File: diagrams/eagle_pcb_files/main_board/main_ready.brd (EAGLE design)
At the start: 67 x 31.5 mm, 31 parts

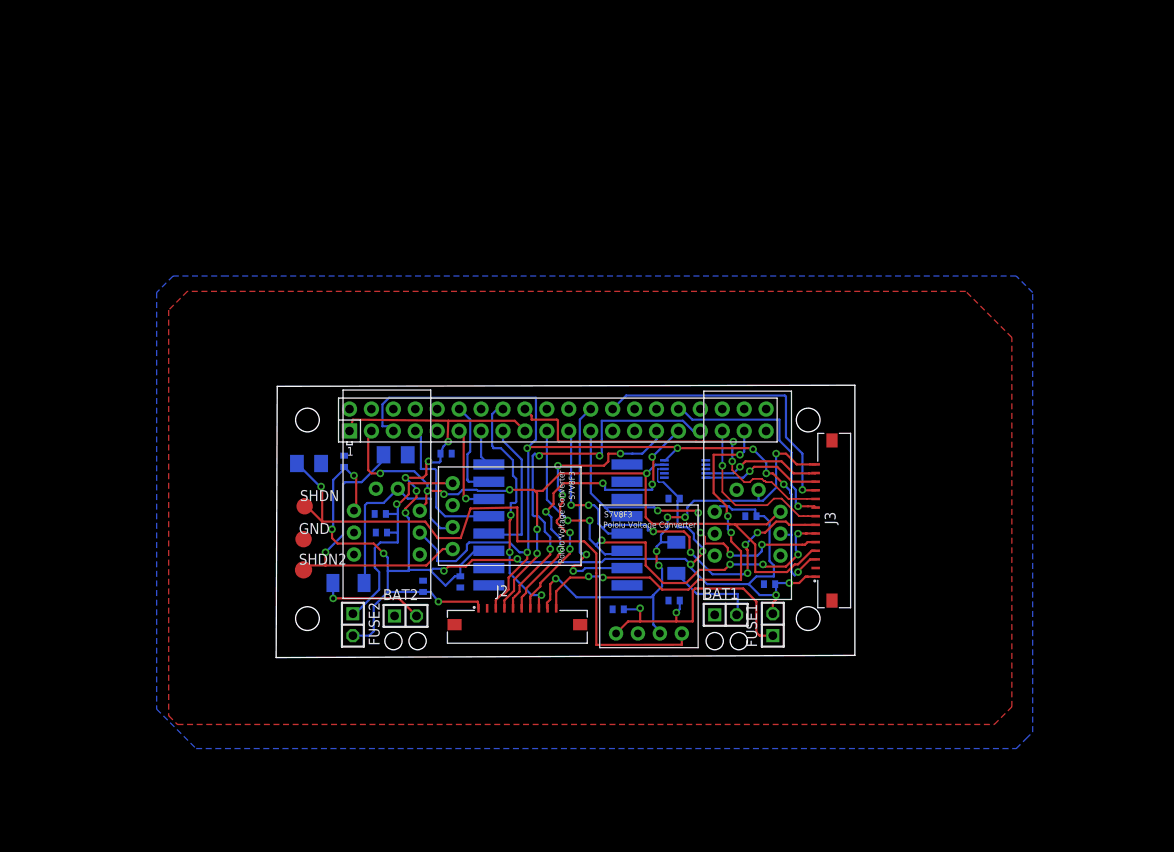
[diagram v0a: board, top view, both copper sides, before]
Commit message: Main board with wider routes and slightly less vias
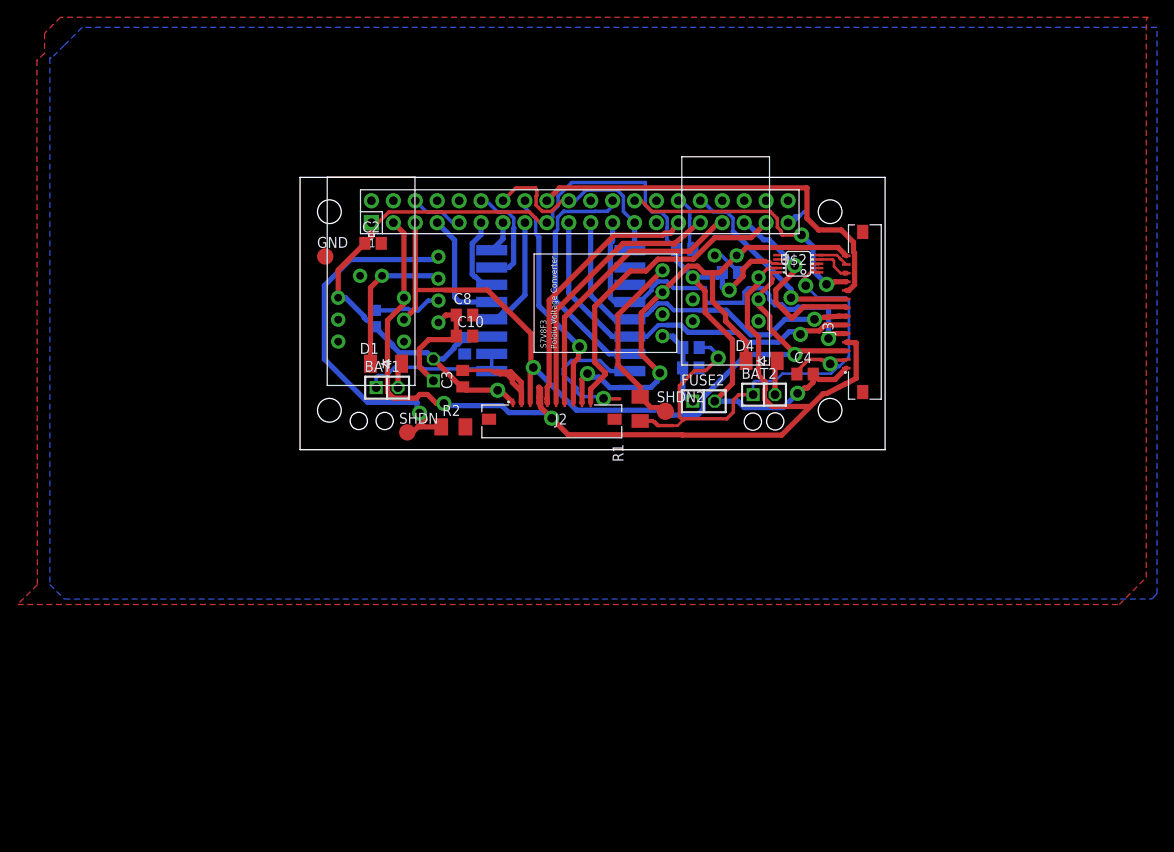
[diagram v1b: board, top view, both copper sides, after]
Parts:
- C1, C2, C3, C4, C6, C7: value (none) -> 100nF; device rcl:C0402 -> rcl:C0805
- C10, C11, C8, C9: device rcl:C0402 -> rcl:C0805
- C5: value 100 nF -> 100nF; device rcl:C0402 -> rcl:C0805
- R1, R2: value (none) -> 4.7k
- moved D4 54.3 mm to (108.2, 37.2), flipped to the top
- moved U$3 50.2 mm to (62.9, 38.1)
- moved C7 49.2 mm to (63.3, 42.1), turned to 90 degrees
- moved FUSE1 49.2 mm to (70.2, 36.1), flipped to the bottom
- moved BAT2 48.8 mm to (108.5, 33.2)
- moved FUSE2 48.2 mm to (101.5, 32.5), turned to 0 degrees
- moved U$9 47.6 mm to (104.0, 40.5)
- moved BAT1 47.2 mm to (64.8, 34.1)
- moved C6 46.5 mm to (99.3, 50.1), turned to 180 degrees
- moved SHDN2 45.8 mm to (97.0, 31.3)
- moved C8 41.0 mm to (73.8, 42.5), flipped to the top
- moved C9 40.8 mm to (100.0, 38.7), turned to 0 degrees
- moved C11 40.6 mm to (100.0, 36.3), turned to 0 degrees
- moved D1 40.5 mm to (64.7, 36.8), flipped to the top, turned to 0 degrees
- moved RAO3 38.0 mm to (77.1, 45.4), flipped to the bottom, turned to 90 degrees
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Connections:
- net A0: now also J3.12; no longer J3.13
- net A1: now also J3.13; no longer J3.12
- net B1: now also RAO2.33; no longer RAO2.29
- net B3: now also RAO2.29; no longer RAO2.33
- net GND: now also RAO2.14, U$2.1
- net VIN1: no longer J2.9, J3.14
- net VIN2: now also J2.9, J3.14
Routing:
- net GND: track 0.00 -> 176.1 mm, vias 0 -> 4
- net 3.3V: track 190.3 -> 144.9 mm, vias 15 -> 3
- net VIN1: track 57.9 -> 17.4 mm, vias 6 -> 0
- net VIN2: track 23.3 -> 61.4 mm, vias 0 -> 2
- net SHDN: track 72.3 -> 43.7 mm
- net SCL: track 115.1 -> 90.7 mm, vias 7 -> 2
- net SDA: track 96.6 -> 116.0 mm, vias 7 -> 2
- net VOUT1: track 32.8 -> 14.1 mm, vias 2 -> 0
- net VOUT2: track 27.5 -> 9.97 mm, vias 1 -> 0
- net SHDN2: track 35.0 -> 21.5 mm, vias 1 -> 0
- net B3: track 44.8 -> 31.4 mm, vias 3 -> 0
- net BUZ: track 47.1 -> 36.2 mm, vias 5 -> 0
- net A1: track 14.0 -> 3.67 mm, vias 1 -> 0
- net MOSI: track 54.9 -> 44.9 mm, vias 7 -> 1
- net A0: track 13.9 -> 4.22 mm, vias 1 -> 0
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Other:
- board size 67 x 31.5 mm -> 67.8 x 31.5 mm

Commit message: prepare main board for production
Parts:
- moved C5 1.42 mm to (103.1, 47.4)
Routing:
- net GND: track 176.1 -> 190.1 mm, vias 4 -> 5
- net DIO1: track 9.23 -> 11.0 mm
- net 3.3V: track 144.9 -> 146.6 mm
- net SCK: track 46.3 -> 47.5 mm
- net RESET: track 13.4 -> 14.2 mm
- net G3: track 47.0 -> 47.7 mm
- net G1: track 22.6 -> 22.0 mm

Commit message: make board-schematic consistent
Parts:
- FUSE1, FUSE2: value (none) -> 1.5A
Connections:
- removed net 5V0@1: RAO2.2
- removed net 5V0@2: RAO2.4
- removed net RX: RAO2.10
- removed net TX: RAO2.8
- new net 5V: RAO2.2, RAO2.4
- net GND: no longer U$2.1
- net VIN2: no longer J2.9, J3.14
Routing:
- net VIN2: track 61.4 -> 37.4 mm, vias 2 -> 1
- net GND: track 190.1 -> 185.7 mm
- net A0: track 4.22 -> 0.00 mm
- net A1: track 3.81 -> 0.00 mm
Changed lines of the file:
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@@
 <attribute name="VALUE" x="105.1306" y="34.7472" size="1.27" layer="27"/>
 </element>
-<element name="FUSE1" library="pinhead" package="1X02" value="" x="70.1548" y="36.1188" smashed="yes" rot="MR90">
+<element name="FUSE1" library="pinhead" package="1X02" value="1.5A" x="70.1548" y="36.1188" smashed="yes" rot="MR90">
 <attribute name="NAME" x="71.9836" y="33.5026" size="1.27" layer="26" ratio="10" rot="MR90"/>
 <attribute name="VALUE" x="66.9798" y="33.5788" size="1.27" layer="28" rot="MR90"/>
 </element>
-<element name="FUSE2" library="pinhead" package="1X02" value="" x="101.473" y="32.4866" smashed="yes">
+<element name="FUSE2" library="pinhead" package="1X02" value="1.5A" x="101.473" y="32.4866" smashed="yes">
 <attribute name="NAME" x="98.8568" y="34.3154" size="1.27" layer="25" ratio="10"/>
 <attribute name="VALUE" x="98.933" y="29.3116" size="1.27" layer="27"/>
@@
 <contactref element="C4" pad="1"/>
 <contactref element="J3" pad="2"/>
-<contactref element="U$2" pad="3"/>
 <contactref element="C5" pad="1"/>
 <contactref element="GND" pad="TP"/>
@@
 <contactref element="RAO1" pad="9"/>
 <contactref element="RAO1" pad="16"/>
-<contactref element="U$2" pad="1"/>
 <contactref element="RAO2" pad="9"/>
 <contactref element="RAO2" pad="39"/>
@@
 <wire x1="81.9912" y1="57.2008" x2="81.8642" y2="57.2008" width="0.4064" layer="1"/>
 <wire x1="81.8642" y1="57.2008" x2="79.7108" y2="57.2008" width="0.4064" layer="1"/>
-<wire x1="79.7108" y1="57.2008" x2="78.22" y2="55.71" width="0.4064" layer="1"/>
 <wire x1="80.3708" y1="32.3038" x2="80.3708" y2="33.599" width="0.6096" layer="1"/>
 <wire x1="79.2988" y1="34.671" x2="79.2988" y2="35.0012" width="0.6096" layer="1"/>
@@
 <wire x1="63.5254" y1="35.2298" x2="63.5254" y2="34.0614" width="0.4064" layer="16"/>
 <wire x1="65.4662" y1="36.2308" x2="64.6938" y2="35.4584" width="0.4064" layer="16"/>
-<wire x1="114.8204" y1="47.4124" x2="113.8204" y2="47.4124" width="0.254" layer="1"/>
-<wire x1="113.8204" y1="47.4124" x2="113.6077" y2="47.1997" width="0.254" layer="1"/>
 <wire x1="113.6077" y1="47.1997" x2="113.087" y2="46.679" width="0.254" layer="1"/>
-<wire x1="114.8204" y1="48.4124" x2="113.6142" y2="48.4124" width="0.254" layer="1"/>
-<wire x1="113.6142" y1="48.4124" x2="113.6077" y2="47.1997" width="0.254" layer="1"/>
 <wire x1="81.8642" y1="57.2008" x2="82.0166" y2="57.0484" width="0.3048" layer="1"/>
 <wire x1="82.0166" y1="57.0484" x2="82.0166" y2="54.8386" width="0.3048" layer="1"/>
@@
 <via x="119.761" y="54.4068" extent="1-16" drill="0.35" diameter="1"/>
 <wire x1="119.634" y1="56.6928" x2="119.8626" y2="56.4642" width="0.6096" layer="16"/>
+<contactref element="U$2" pad="3"/>
+<wire x1="114.8204" y1="48.4124" x2="113.3856" y2="48.4124" width="0.2032" layer="1"/>
 </signal>
 <signal name="NSS">
@@
 <contactref element="D4" pad="C"/>
 <contactref element="U$9" pad="+"/>
-<contactref element="J2" pad="9"/>
 <wire x1="106.3786" y1="37.1602" x2="106.3786" y2="39.3954" width="0.6096" layer="1"/>
 <wire x1="106.3786" y1="39.3954" x2="104.013" y2="41.761" width="0.6096" layer="1"/>
-<contactref element="J3" pad="14"/>
-<wire x1="87.3708" y1="32.3038" x2="87.376" y2="32.309" width="0.6096" layer="1"/>
-<wire x1="103.279575" y1="47.374175" x2="105.283" y2="49.3776" width="0.6096" layer="1"/>
 <wire x1="104.013" y1="41.761" x2="104.013" y2="42.5196" width="0.6096" layer="1"/>
 <wire x1="101.4984" y1="47.374175" x2="100.739575" y2="48.133" width="0.3048" layer="1"/>
@@
 <wire x1="99.666425" y1="48.133" x2="96.6978" y2="45.164375" width="0.3048" layer="1"/>
 <wire x1="101.4984" y1="47.374175" x2="102.489" y2="47.374175" width="0.3048" layer="1"/>
-<wire x1="102.489" y1="47.374175" x2="103.279575" y2="47.374175" width="0.6096" layer="1"/>
-<wire x1="105.5116" y1="49.3776" x2="106.426" y2="50.292" width="0.6096" layer="1"/>
-<wire x1="105.5116" y1="49.3776" x2="105.283" y2="49.3776" width="0.6096" layer="1"/>
-<wire x1="117.0204" y1="50.292" x2="117.988" y2="49.3244" width="0.6096" layer="1"/>
-<wire x1="106.426" y1="50.292" x2="117.0204" y2="50.292" width="0.6096" layer="1"/>
-<wire x1="87.376" y1="35.052" x2="88.011" y2="35.687" width="0.6096" layer="1"/>
-<via x="88.011" y="35.687" extent="1-16" drill="0.3" diameter="1" shape="octagon"/>
-<wire x1="88.011" y1="35.687" x2="88.4174" y2="35.2806" width="0.6096" layer="16"/>
-<wire x1="88.4174" y1="35.2806" x2="89.3826" y2="35.2806" width="0.6096" layer="16"/>
-<wire x1="89.3826" y1="35.2806" x2="90.6018" y2="34.0614" width="0.6096" layer="16"/>
 <wire x1="91.6686" y1="34.0614" x2="91.694" y2="34.0868" width="0.6096" layer="16"/>
-<wire x1="87.376" y1="32.309" x2="87.376" y2="35.052" width="0.6096" layer="1"/>
 <wire x1="90.6018" y1="34.0614" x2="91.6686" y2="34.0614" width="0.6096" layer="16"/>
 <wire x1="91.694" y1="34.0868" x2="95.3516" y2="34.0868" width="0.6096" layer="16"/>
@@
 <wire x1="94.234" y1="42.700575" x2="96.6978" y2="45.164375" width="0.6096" layer="1"/>
 <wire x1="94.234" y1="37.9222" x2="94.234" y2="42.700575" width="0.6096" layer="1"/>
+<wire x1="102.489" y1="47.374175" x2="105.283" y2="49.3776" width="0" layer="19" extent="1-1"/>
 </signal>
 <signal name="SCK">
@@
 <wire x1="109.9954" y1="53.63473125" x2="109.9954" y2="52.336" width="0.3048" layer="1"/>
 </signal>
-<signal name="5V0@1">
-<contactref element="RAO2" pad="2"/>
-</signal>
-<signal name="5V0@2">
-<contactref element="RAO2" pad="4"/>
-</signal>
-<signal name="TX">
-<contactref element="RAO2" pad="8"/>
-</signal>
-<signal name="RX">
-<contactref element="RAO2" pad="10"/>
-</signal>
 <signal name="SHDN">
 <contactref element="RAO3" pad="SHDN"/>
@@
 <contactref element="U$2" pad="4"/>
 <contactref element="J3" pad="12"/>
-<wire x1="117.7798" y1="47.3244" x2="117.3268" y2="47.3244" width="0.3048" layer="1"/>
-<wire x1="117.3268" y1="47.3244" x2="117.3226" y2="47.3202" width="0.3048" layer="1"/>
-<wire x1="117.3226" y1="47.3202" x2="116.5606" y2="48.0822" width="0.3048" layer="1"/>
-<wire x1="116.5606" y1="48.0822" x2="116.5606" y2="48.7426" width="0.3048" layer="1"/>
-<wire x1="116.3908" y1="48.9124" x2="116.5606" y2="48.7426" width="0.3048" layer="1"/>
-<wire x1="117.988" y1="47.3244" x2="117.7798" y2="47.3244" width="0.6096" layer="1"/>
-<wire x1="114.8204" y1="48.9124" x2="116.3908" y2="48.9124" width="0.254" layer="1"/>
+<wire x1="117.988" y1="47.3244" x2="114.8204" y2="48.9124" width="0" layer="19" extent="1-1"/>
 </signal>
 <signal name="A1">
 <contactref element="U$2" pad="5"/>
 <contactref element="J3" pad="13"/>
-<wire x1="114.8204" y1="49.4124" x2="116.9" y2="49.4124" width="0.254" layer="1"/>
-<wire x1="116.9" y1="49.4124" x2="116.9" y2="49.089" width="0.254" layer="1"/>
-<wire x1="117.6646" y1="48.3244" x2="117.988" y2="48.3244" width="0.254" layer="1"/>
-<wire x1="116.9" y1="49.089" x2="117.6646" y2="48.3244" width="0.254" layer="1"/>
+<wire x1="114.8204" y1="49.4124" x2="117.988" y2="48.3244" width="0" layer="19" extent="1-1"/>
 </signal>
 <signal name="BUZ">
@@
 <wire x1="89.6112" y1="36.2458" x2="89.6112" y2="35.1282" width="0.3048" layer="1"/>
 </signal>
+<signal name="5V">
+<contactref element="RAO2" pad="4"/>
+<contactref element="RAO2" pad="2"/>
+<wire x1="62.98" y1="55.71" x2="65.52" y2="55.71" width="0" layer="19" extent="1-1"/>
+</signal>
 </signals>

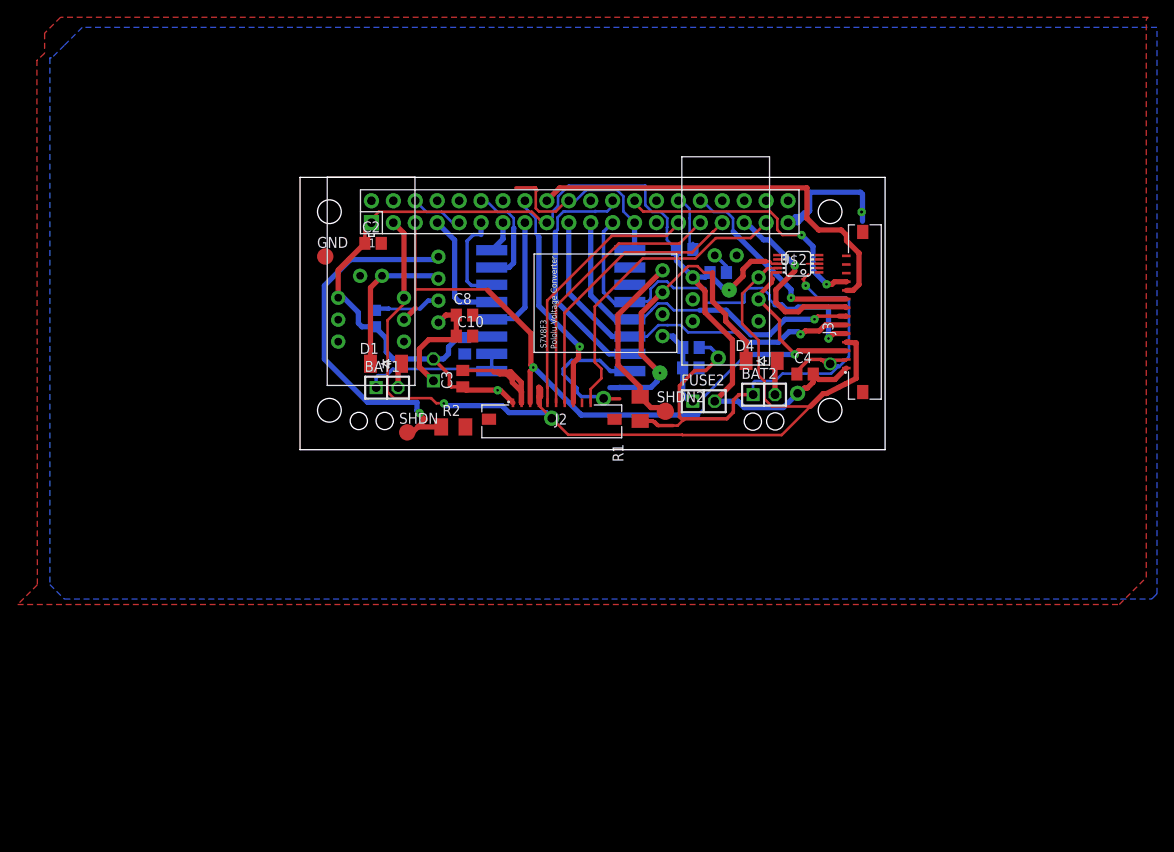
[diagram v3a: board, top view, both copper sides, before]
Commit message: remove res from safetypin, fix fuel gauge circuit, add jumper to ommit fuel gauge
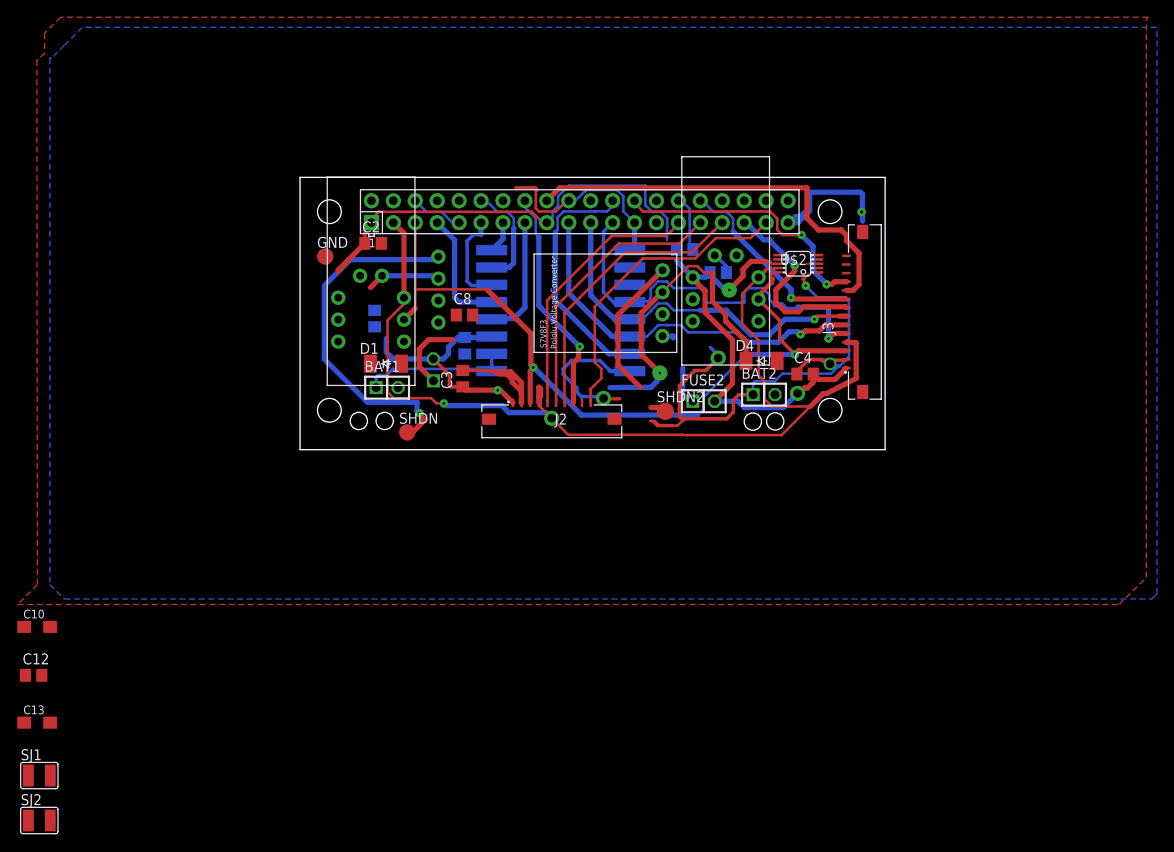
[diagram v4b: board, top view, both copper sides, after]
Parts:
- removed C11: 10 uF, rcl:C0805
- removed C9: 100 nF, rcl:C0805
- removed R1, R2: 4.7k, rcl:M1206
- added C12: 100 nF, rcl:C0805
- added C13: 10uF, rcl:SMC_A
- added SJ1, SJ2: (no value), jumper:SJW
- C10: value 10 uF -> 10uF; device rcl:C0805 -> rcl:SMC_A
- moved C10 59.9 mm to (24.3, 6.35)
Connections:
- removed net SHDN: R2.1, RAO3.SHDN, SHDN.TP
- new net A: D1.C, RAO3.VIN
- new net B: D4.C, RAO4.VIN
- new net SHDN1: RAO3.SHDN, SHDN.TP
- net 3.3V: no longer C6.1, C7.1, U$3.VCC, U$9.VCC
- net BIN1: now also SJ1.1, U$3.+; no longer D1.A
- net BIN2: now also SJ2.1, U$9.+; no longer D4.A
- net GND: now also C10.-, C12.2, C13.-, C6.1; no longer C10.2, C11.1, C6.2, C9.1, R1.1, R2.2
- net SHDN2: no longer R1.2
- net VIN1: now also C7.1, D1.A, SJ1.2, U$3.VCC; no longer D1.C, RAO3.VIN, U$3.+
- net VIN2: now also C6.2, D4.A, J3.14, SJ2.2, U$9.VCC; no longer D4.C, RAO4.VIN, U$9.+
- net VOUT1: now also C10.+; no longer C10.1
- net VOUT2: now also C12.1, C13.+; no longer C11.2, C9.2
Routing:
- net SHDN: track 43.7 -> 0.00 mm, vias 1 -> 0
- net SHDN1: track 0.00 -> 41.0 mm, vias 0 -> 1
- net VIN2: track 37.4 -> 0.00 mm, vias 1 -> 0
- net B: track 0.00 -> 37.4 mm, vias 0 -> 1
- net VIN1: track 17.4 -> 0.00 mm
- net 3.3V: track 146.6 -> 131.8 mm
- net GND: track 185.7 -> 171.3 mm
- net VOUT1: track 14.1 -> 8.68 mm
- net BIN1: track 2.94 -> 8.12 mm
- net BIN2: track 4.02 -> 0.00 mm
- net VOUT2: track 9.97 -> 5.99 mm
- net SHDN2: track 21.5 -> 18.6 mm
